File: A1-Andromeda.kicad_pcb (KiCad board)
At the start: 2 copper layers, 44 x 79.3 mm, 39 parts, among them J1 Conn_01x02, J2 Conn_01x02, J3 Conn_01x02, J5 Conn_01x10_Pin, J6 Conn_01x10_Pin, J8 Conn_01x10_Pin, SW1 SW_SPST, SW2 SW_DIP_x02, U1 LM2940IMPX-5.0/NOPB, U2 NUCLEO-F042K6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

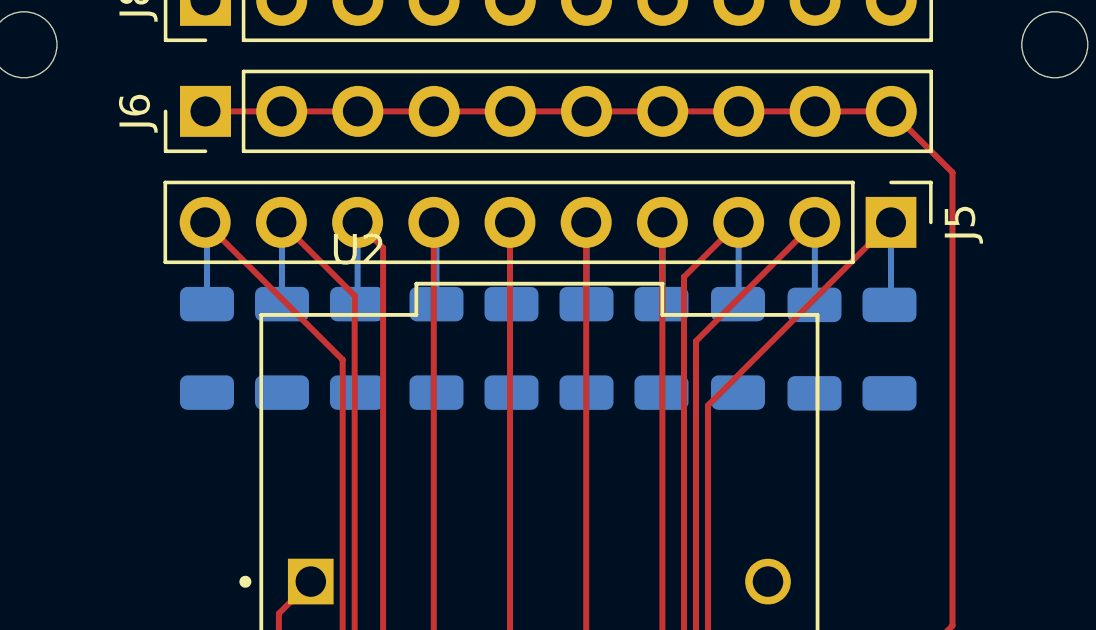
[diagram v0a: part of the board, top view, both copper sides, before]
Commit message: remove bypass capacitors
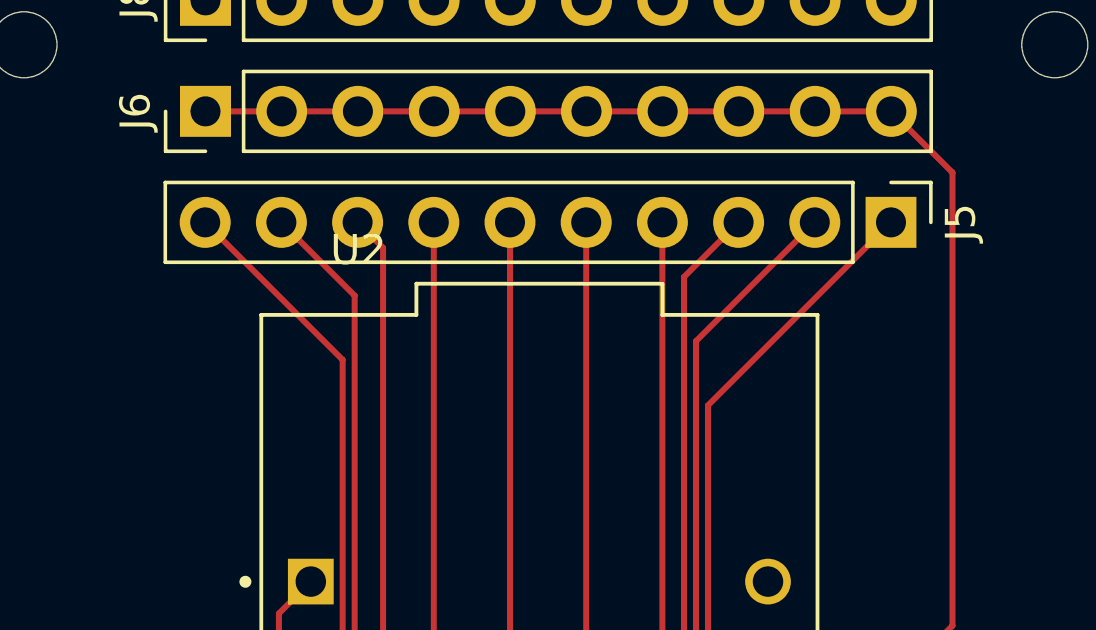
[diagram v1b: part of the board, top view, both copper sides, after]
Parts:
- removed C10, C11, C12, C13, C14, C15, C16, C17, C4, C6: 0.1uF, Capacitor_SMD:C_1206_3216Metric
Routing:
- net /A7: track 28.2 -> 25.5 mm
- net /A6: track 30.0 -> 27.3 mm
- net /A3: track 37.5 -> 34.8 mm
- net /D4: track 31.3 -> 28.6 mm
- net /D3: track 29.0 -> 26.3 mm
- net /A5: track 31.8 -> 29.1 mm
- net /A4: track 33.9 -> 31.2 mm
- net /D6: track 37.7 -> 35.0 mm
- net /D2: track 27.1 -> 24.5 mm
- net /D5: track 34.1 -> 31.5 mm

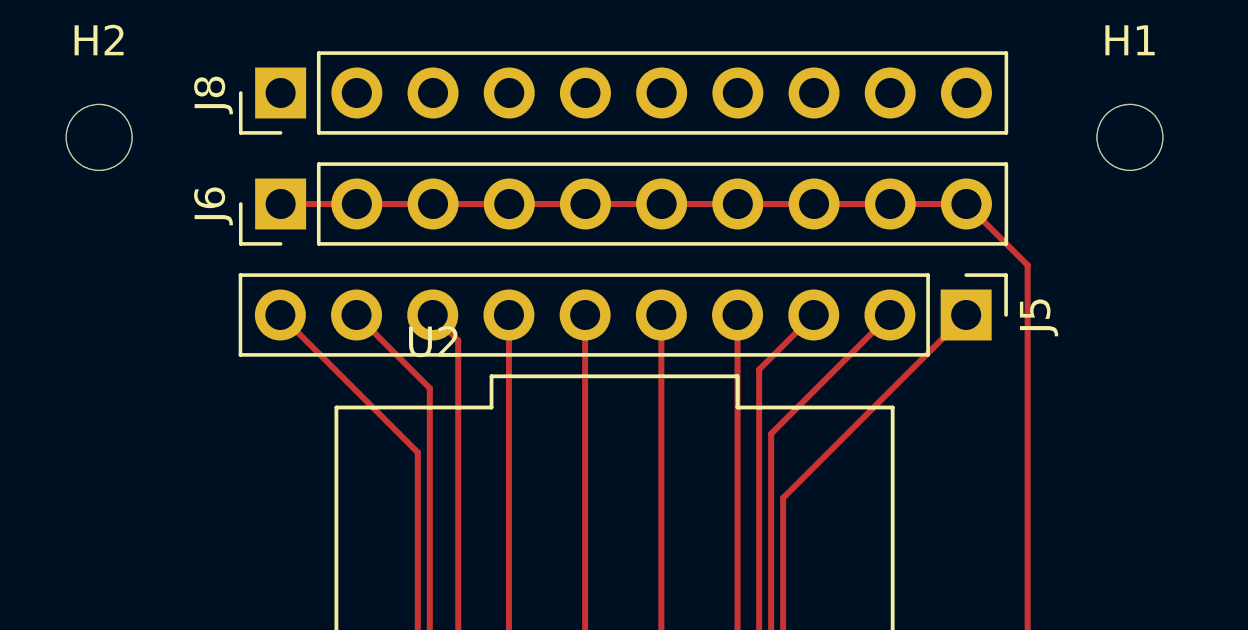
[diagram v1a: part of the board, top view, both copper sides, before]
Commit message: rotate GPIO pin array
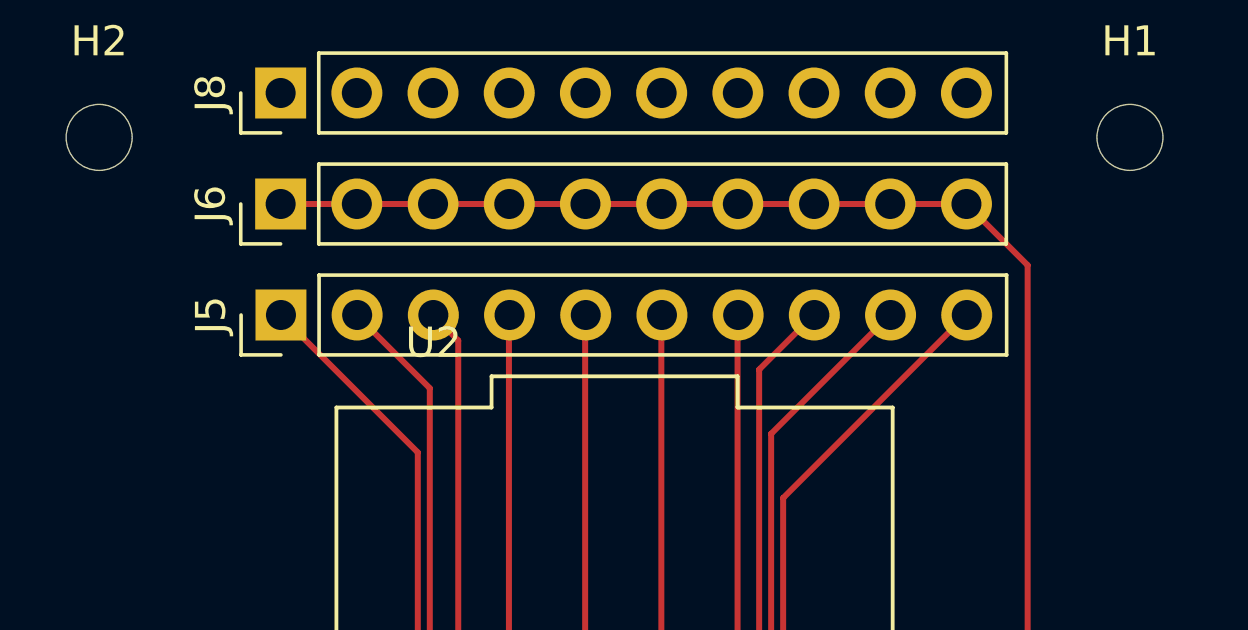
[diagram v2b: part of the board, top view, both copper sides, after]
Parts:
- moved J5 22.8 mm to (140.6, 64.9), turned to 90 degrees
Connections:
- J5 pad 1: /A7 -> /D2
- J5 pad 10: /D2 -> /A7
- J5 pad 2: /A6 -> /D3
- J5 pad 3: /A5 -> /D4
- J5 pad 4: /A4 -> /D5
- J5 pad 5: /A3 -> /D6
- J5 pad 6: /D6 -> /A3
- J5 pad 7: /D5 -> /A4
- J5 pad 8: /D4 -> /A5
- J5 pad 9: /D3 -> /A6
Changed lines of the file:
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@@
 	(footprint "Connector_PinHeader_2.54mm:PinHeader_1x10_P2.54mm_Vertical"
 		(layer "F.Cu")
-		(at 163.4 64.9 -90)
+		(at 140.56 64.9 90)
 		(descr "Through hole straight pin header, 1x10, 2.54mm pitch, single row")
 		(tags "Through hole pin header THT 1x10 2.54mm single row")
@@
 		)
 		(property "Footprint" "Connector_PinHeader_2.54mm:PinHeader_1x10_P2.54mm_Vertical"
-			(at 0 0 -90)
+			(at 0 0 90)
 			(unlocked yes)
 			(layer "F.Fab")
@@
 		)
 		(property "Datasheet" ""
-			(at 0 0 -90)
+			(at 0 0 90)
 			(unlocked yes)
 			(layer "F.Fab")
@@
 		)
 		(property "Description" "Generic connector, single row, 01x10, script generated"
-			(at 0 0 -90)
+			(at 0 0 90)
 			(unlocked yes)
 			(layer "F.Fab")
@@
 		(attr through_hole)
 		(fp_line
+			(start -1.33 -1.33)
+			(end 0 -1.33)
+			(stroke
+				(width 0.12)
+				(type solid)
+			)
+			(layer "F.SilkS")
+		)
+		(fp_line
+			(start -1.33 0)
+			(end -1.33 -1.33)
+			(stroke
+				(width 0.12)
+				(type solid)
+			)
+			(layer "F.SilkS")
+		)
+		(fp_line
+			(start 1.33 1.27)
+			(end 1.33 24.19)
+			(stroke
+				(width 0.12)
+				(type solid)
+			)
+			(layer "F.SilkS")
+		)
+		(fp_line
+			(start -1.33 1.27)
+			(end 1.33 1.27)
+			(stroke
+				(width 0.12)
+				(type solid)
+			)
+			(layer "F.SilkS")
+		)
+		(fp_line
+			(start -1.33 1.27)
+			(end -1.33 24.19)
+			(stroke
+				(width 0.12)
+				(type solid)
+			)
+			(layer "F.SilkS")
+		)
+		(fp_line
 			(start -1.33 24.19)
 			(end 1.33 24.19)
@@
 		)
 		(fp_line
-			(start -1.33 1.27)
-			(end -1.33 24.19)
-			(stroke
-				(width 0.12)
-				(type solid)
-			)
-			(layer "F.SilkS")
-		)
-		(fp_line
-			(start -1.33 1.27)
-			(end 1.33 1.27)
-			(stroke
-				(width 0.12)
-				(type solid)
-			)
-			(layer "F.SilkS")
-		)
-		(fp_line
-			(start 1.33 1.27)
-			(end 1.33 24.19)
-			(stroke
-				(width 0.12)
-				(type solid)
-			)
-			(layer "F.SilkS")
-		)
-		(fp_line
-			(start -1.33 0)
-			(end -1.33 -1.33)
-			(stroke
-				(width 0.12)
-				(type solid)
-			)
-			(layer "F.SilkS")
-		)
-		(fp_line
-			(start -1.33 -1.33)
-			(end 0 -1.33)
-			(stroke
-				(width 0.12)
-				(type solid)
-			)
-			(layer "F.SilkS")
+			(start 1.8 -1.8)
+			(end -1.8 -1.8)
+			(stroke
+				(width 0.05)
+				(type solid)
+			)
+			(layer "F.CrtYd")
+		)
+		(fp_line
+			(start -1.8 -1.8)
+			(end -1.8 24.65)
+			(stroke
+				(width 0.05)
+				(type solid)
+			)
+			(layer "F.CrtYd")
+		)
+		(fp_line
+			(start 1.8 24.65)
+			(end 1.8 -1.8)
+			(stroke
+				(width 0.05)
+				(type solid)
+			)
+			(layer "F.CrtYd")
 		)
 		(fp_line
@@
 		)
 		(fp_line
-			(start 1.8 24.65)
-			(end 1.8 -1.8)
-			(stroke
-				(width 0.05)
-				(type solid)
-			)
-			(layer "F.CrtYd")
-		)
-		(fp_line
-			(start -1.8 -1.8)
-			(end -1.8 24.65)
-			(stroke
-				(width 0.05)
-				(type solid)
-			)
-			(layer "F.CrtYd")
-		)
-		(fp_line
-			(start 1.8 -1.8)
-			(end -1.8 -1.8)
-			(stroke
-				(width 0.05)
-				(type solid)
-			)
-			(layer "F.CrtYd")
+			(start 1.27 -1.27)
+			(end 1.27 24.13)
+			(stroke
+				(width 0.1)
+				(type solid)
+			)
+			(layer "F.Fab")
+		)
+		(fp_line
+			(start -0.635 -1.27)
+			(end 1.27 -1.27)
+			(stroke
+				(width 0.1)
+				(type solid)
+			)
+			(layer "F.Fab")
+		)
+		(fp_line
+			(start -1.27 -0.635)
+			(end -0.635 -1.27)
+			(stroke
+				(width 0.1)
+				(type solid)
+			)
+			(layer "F.Fab")
+		)
+		(fp_line
+			(start 1.27 24.13)
+			(end -1.27 24.13)
+			(stroke
+				(width 0.1)
+				(type solid)
+			)
+			(layer "F.Fab")
 		)
 		(fp_line
@@
 			(layer "F.Fab")
 		)
-		(fp_line
-			(start 1.27 24.13)
-			(end -1.27 24.13)
-			(stroke
-				(width 0.1)
-				(type solid)
-			)
-			(layer "F.Fab")
-		)
-		(fp_line
-			(start -1.27 -0.635)
-			(end -0.635 -1.27)
-			(stroke
-				(width 0.1)
-				(type solid)
-			)
-			(layer "F.Fab")
-		)
-		(fp_line
-			(start -0.635 -1.27)
-			(end 1.27 -1.27)
-			(stroke
-				(width 0.1)
-				(type solid)
-			)
-			(layer "F.Fab")
-		)
-		(fp_line
-			(start 1.27 -1.27)
-			(end 1.27 24.13)
-			(stroke
-				(width 0.1)
-				(type solid)
-			)
-			(layer "F.Fab")
-		)
 		(fp_text user "${REFERENCE}"
-			(at 0 11.43 0)
+			(at 0 11.43 360)
 			(layer "F.Fab")
 			(effects
@@
 		)
 		(pad "1" thru_hole rect
-			(at 0 0 270)
+			(at 0 0 90)
+			(size 1.7 1.7)
+			(drill 1)
+			(layers "*.Cu" "*.Mask")
+			(remove_unused_layers no)
+			(net 11 "/D2")
+			(pinfunction "Pin_1")
+			(pintype "passive")
+		)
+		(pad "2" thru_hole oval
+			(at 0 2.54 90)
+			(size 1.7 1.7)
+			(drill 1)
+			(layers "*.Cu" "*.Mask")
+			(remove_unused_layers no)
+			(net 12 "/D3")
+			(pinfunction "Pin_2")
+			(pintype "passive")
+		)
+		(pad "3" thru_hole oval
+			(at 0 5.08 90)
+			(size 1.7 1.7)
+			(drill 1)
+			(layers "*.Cu" "*.Mask")
+			(remove_unused_layers no)
+			(net 17 "/D4")
+			(pinfunction "Pin_3")
+			(pintype "passive")
+		)
+		(pad "4" thru_hole oval
+			(at 0 7.62 90)
+			(size 1.7 1.7)
+			(drill 1)
+			(layers "*.Cu" "*.Mask")
+			(remove_unused_layers no)
+			(net 18 "/D5")
+			(pinfunction "Pin_4")
+			(pintype "passive")
+		)
+		(pad "5" thru_hole oval
+			(at 0 10.16 90)
+			(size 1.7 1.7)
+			(drill 1)
+			(layers "*.Cu" "*.Mask")
+			(remove_unused_layers no)
+			(net 39 "/D6")
+			(pinfunction "Pin_5")
+			(pintype "passive")
+		)
+		(pad "6" thru_hole oval
+			(at 0 12.7 90)
+			(size 1.7 1.7)
+			(drill 1)
+			(layers "*.Cu" "*.Mask")
+			(remove_unused_layers no)
+			(net 10 "/A3")
+			(pinfunction "Pin_6")
+			(pintype "passive")
+		)
+		(pad "7" thru_hole oval
+			(at 0 15.24 90)
+			(size 1.7 1.7)
+			(drill 1)
+			(layers "*.Cu" "*.Mask")
+			(remove_unused_layers no)
+			(net 13 "/A4")
+			(pinfunction "Pin_7")
+			(pintype "passive")
+		)
+		(pad "8" thru_hole oval
+			(at 0 17.78 90)
+			(size 1.7 1.7)
+			(drill 1)
+			(layers "*.Cu" "*.Mask")
+			(remove_unused_layers no)
+			(net 9 "/A5")
+			(pinfunction "Pin_8")
+			(pintype "passive")
+		)
+		(pad "9" thru_hole oval
+			(at 0 20.32 90)
+			(size 1.7 1.7)
+			(drill 1)
+			(layers "*.Cu" "*.Mask")
+			(remove_unused_layers no)
+			(net 19 "/A6")
+			(pinfunction "Pin_9")
+			(pintype "passive")
+		)
+		(pad "10" thru_hole oval
+			(at 0 22.86 90)
 			(size 1.7 1.7)
 			(drill 1)
@@
 			(remove_unused_layers no)
 			(net 16 "/A7")
-			(pinfunction "Pin_1")
-			(pintype "passive")
-		)
-		(pad "2" thru_hole oval
-			(at 0 2.54 270)
-			(size 1.7 1.7)
-			(drill 1)
-			(layers "*.Cu" "*.Mask")
-			(remove_unused_layers no)
-			(net 19 "/A6")
-			(pinfunction "Pin_2")
-			(pintype "passive")
-		)
-		(pad "3" thru_hole oval
-			(at 0 5.08 270)
-			(size 1.7 1.7)
-			(drill 1)
-			(layers "*.Cu" "*.Mask")
-			(remove_unused_layers no)
-			(net 9 "/A5")
-			(pinfunction "Pin_3")
-			(pintype "passive")
-		)
-		(pad "4" thru_hole oval
-			(at 0 7.62 270)
-			(size 1.7 1.7)
-			(drill 1)
-			(layers "*.Cu" "*.Mask")
-			(remove_unused_layers no)
-			(net 13 "/A4")
-			(pinfunction "Pin_4")
-			(pintype "passive")
-		)
-		(pad "5" thru_hole oval
-			(at 0 10.16 270)
-			(size 1.7 1.7)
-			(drill 1)
-			(layers "*.Cu" "*.Mask")
-			(remove_unused_layers no)
-			(net 10 "/A3")
-			(pinfunction "Pin_5")
-			(pintype "passive")
-		)
-		(pad "6" thru_hole oval
-			(at 0 12.7 270)
-			(size 1.7 1.7)
-			(drill 1)
-			(layers "*.Cu" "*.Mask")
-			(remove_unused_layers no)
-			(net 39 "/D6")
-			(pinfunction "Pin_6")
-			(pintype "passive")
-		)
-		(pad "7" thru_hole oval
-			(at 0 15.24 270)
-			(size 1.7 1.7)
-			(drill 1)
-			(layers "*.Cu" "*.Mask")
-			(remove_unused_layers no)
-			(net 18 "/D5")
-			(pinfunction "Pin_7")
-			(pintype "passive")
-		)
-		(pad "8" thru_hole oval
-			(at 0 17.78 270)
-			(size 1.7 1.7)
-			(drill 1)
-			(layers "*.Cu" "*.Mask")
-			(remove_unused_layers no)
-			(net 17 "/D4")
-			(pinfunction "Pin_8")
-			(pintype "passive")
-		)
-		(pad "9" thru_hole oval
-			(at 0 20.32 270)
-			(size 1.7 1.7)
-			(drill 1)
-			(layers "*.Cu" "*.Mask")
-			(remove_unused_layers no)
-			(net 12 "/D3")
-			(pinfunction "Pin_9")
-			(pintype "passive")
-		)
-		(pad "10" thru_hole oval
-			(at 0 22.86 270)
-			(size 1.7 1.7)
-			(drill 1)
-			(layers "*.Cu" "*.Mask")
-			(remove_unused_layers no)
-			(net 11 "/D2")
 			(pinfunction "Pin_10")
 			(pintype "passive")

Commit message: fix ground plane
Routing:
- net GND: track 13.4 -> 1.12 mm
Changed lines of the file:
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@@
 		)
 		(fp_text user "${REFERENCE}"
-			(at 0 11.43 360)
+			(at 0 11.43 0)
 			(layer "F.Fab")
 			(effects
@@
 	)
 	(segment
-		(start 134.26 96.555)
-		(end 137.615 93.2)
-		(width 2)
-		(layer "B.Cu")
-		(net 38)
-	)
-	(segment
-		(start 167.965 93.2)
-		(end 169.55 93.2)
-		(width 2)
-		(layer "B.Cu")
-		(net 38)
-	)
-	(segment
-		(start 137.615 93.2)
-		(end 139 93.2)
-		(width 2)
-		(layer "B.Cu")
-		(net 38)
-	)
-	(segment
-		(start 164.76 96.405)
-		(end 167.965 93.2)
-		(width 2)
-		(layer "B.Cu")
-		(net 38)
-	)
-	(segment
 		(start 150.7 64.9)
 		(end 150.7 90.554)
@@
 		(polygon
 			(pts
-				(xy 165.1 97.525) (xy 165.1 95.2) (xy 164.45 95.225) (xy 164.425 97.525)
+				(xy 165.1 97.525) (xy 165.1 95.2) (xy 164.45 95.2) (xy 164.425 97.525)
 			)
 		)
@@
 			)
 		)
-	)
-	(zone
-		(net 0)
-		(net_name "")
-		(layer "B.Cu")
-		(hatch edge 0.5)
-		(connect_pads yes
-			(clearance 0)
-		)
-		(min_thickness 0.25)
-		(filled_areas_thickness no)
-		(keepout
-			(tracks allowed)
-			(vias allowed)
-			(pads allowed)
-			(copperpour not_allowed)
-			(footprints allowed)
-		)
-		(fill
-			(thermal_gap 0.5)
-			(thermal_bridge_width 0.5)
-			(island_removal_mode 1)
-			(island_area_min 10)
-		)
-		(polygon
-			(pts
-				(xy 170.65 94.325) (xy 168.55 94.325) (xy 165.25 97.625) (xy 163.85 97.275) (xy 163.55 95.975) (xy 167.4 92.125)
-				(xy 167.75 92.125) (xy 170.65 92.125)
-			)
-		)
-	)
-	(zone
-		(net 0)
-		(net_name "")
-		(layer "B.Cu")
-		(hatch edge 0.5)
-		(connect_pads yes
-			(clearance 0)
-		)
-		(min_thickness 0.25)
-		(filled_areas_thickness no)
-		(keepout
-			(tracks allowed)
-			(vias allowed)
-			(pads allowed)
-			(copperpour not_allowed)
-			(footprints allowed)
-		)
-		(fill
-			(thermal_gap 0.5)
-			(thermal_bridge_width 0.5)
-			(island_removal_mode 1)
-			(island_area_min 10)
-		)
-		(polygon
-			(pts
-				(xy 140.15 94.475) (xy 138.05 94.475) (xy 134.55 97.9) (xy 133.45 97.475) (xy 132.85 96.35) (xy 136.8 92.375)
-				(xy 137.3 92.025) (xy 140.2 92.025)
-			)
-		)

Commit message: redo PCB
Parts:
- moved H4 85.7 mm to (104.2, 71.9)
- moved H3 79.2 mm to (190.2, 71.9)
- moved H1 77.6 mm to (104.2, 101.9)
- moved H2 70.3 mm to (190.2, 101.9)
- moved J1 67.9 mm to (111.1, 81.2), turned to 0 degrees
- moved C3 61.6 mm to (117.0, 75.6), turned to 180 degrees
- moved C1 60.9 mm to (185.1, 85.1)
- moved SW1 58.6 mm to (123.9, 74.3), turned to 90 degrees
- moved U1 55.6 mm to (187.2, 90.0), turned to 0 degrees
- moved C2 52.0 mm to (185.1, 94.9), turned to 0 degrees
- moved F1 50.3 mm to (117.0, 73.1)
- moved TP2 40.2 mm to (168.2, 75.3)
- moved SW2 34.6 mm to (177.3, 98.2), turned to 180 degrees
- moved TP1 32.6 mm to (184.3, 82.2)
- moved R2 30.4 mm to (179.9, 75.6), turned to 0 degrees
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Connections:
- J5 pad 1: /D2 -> /D6
- J5 pad 2: /D3 -> /D5
- J5 pad 4: /D5 -> /D3
- J5 pad 5: /D6 -> /D2
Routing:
- net +5V: track 136.4 -> 79.4 mm, vias 1 -> 2
- net +12V: track 82.9 -> 121.2 mm
- net /D6: track 35.0 -> 4.46 mm
- net /L_MOTOR_IN2: track 11.4 -> 38.7 mm, vias 2 -> 0
- net /D5: track 31.5 -> 4.46 mm
- net /R_MOTOR_IN2: track 47.8 -> 22.3 mm
- net /D4: track 28.6 -> 4.46 mm
- net /R_MOTOR_IN1: track 47.2 -> 23.6 mm
- net /L_MOTOR_IN1: track 11.5 -> 34.0 mm
- net /D3: track 26.3 -> 4.46 mm
- net /D2: track 24.5 -> 4.46 mm
- net /DIP_SWITCH_OUT1: track 38.2 -> 55.8 mm, vias 4 -> 0
- net /DIP_SWITCH_OUT2: track 39.1 -> 50.6 mm, vias 4 -> 0
- net Net-(J3-Pin_1): track 15.3 -> 4.66 mm
- net /A3: track 34.8 -> 25.0 mm
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- removed copper zone on F.Cu, net Net-(U3-ILIM)
- removed copper zone on F.Cu, net Net-(U4-ILIM)
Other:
- board size 44 x 79.3 mm -> 96 x 40 mm

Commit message: update silkscreen
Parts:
- moved GND 50.0 mm to (184.0, 69.2)
- moved SW2 35.7 mm to (141.8, 102.8)
- moved 12V 14.0 mm to (179.0, 69.2)
- moved 5V 8.38 mm to (174.0, 69.2)
- moved J1 1.91 mm to (109.2, 81.0)
- moved J3 0.79 mm to (176.8, 87.5)
- moved C8 0.79 mm to (172.5, 82.3)
- moved J5 0.79 mm to (140.8, 77.4)
- moved J6 0.79 mm to (140.8, 73.7)
- moved J8 0.79 mm to (140.8, 69.9)
- moved U4 0.79 mm to (179.2, 80.7)
- moved C5 0.79 mm to (116.6, 100.4)
- moved R1 0.79 mm to (110.9, 103.4)
- moved C3 0.79 mm to (116.3, 75.2)
- moved F1 0.79 mm to (116.3, 72.7)
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- renumbered TP1 to 12V, TP2 to 5V, TP3 to GND
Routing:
- net /DIP_SWITCH_OUT1: track 55.8 -> 23.4 mm
- net /DIP_SWITCH_OUT2: track 50.6 -> 20.0 mm
- net +5V: track 79.4 -> 99.8 mm, vias 2 -> 4
- net +12V: track 121.2 -> 126.9 mm
- net (no net): track 5.37 -> 0.00 mm
- net /R_MOTOR_IN2: track 22.3 -> 21.5 mm
- net Net-(J2-Pin_2): track 10.4 -> 9.67 mm
- net /R_MOTOR_IN1: track 23.6 -> 22.9 mm
- net Net-(J1-Pin_2): track 12.5 -> 13.2 mm
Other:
- board text added: "5V"
- board text added: "A3"
- board text added: "A4"
- board text added: "A5"
- board text added: "A6"
- board text added: "A7"
- board text added: "D2"
- board text added: "D3"
- board text added: "D4"
- board text added: "D5"
- board text added: "D6"
- board text added: "GND"
- board text added: "GPIO"
- board text added: "L"
- board text added: "MODE"
- board text added: "R"

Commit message: finish up
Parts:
- added D1: GREEN, LED_SMD:LED_1206_3216Metric, F.Cu at (113.9, 69.6)
- added J4: Conn_01x03_Socket, Connector_PinSocket_2.54mm:PinSocket_1x03_P2.54mm_Vertical, F.Cu at (129.3, 102.0)
- added R3: 100K, Capacitor_SMD:C_1206_3216Metric, F.Cu at (134.6, 101.5)
- added R4: 100K, Capacitor_SMD:C_1206_3216Metric, F.Cu at (134.6, 103.9)
- added R5: 220, Resistor_SMD:R_1206_3216Metric, F.Cu at (116.3, 69.6)
- moved R2 28.8 mm to (174.7, 103.7), turned to 180 degrees
- moved C7 23.6 mm to (180.5, 100.8), turned to 180 degrees
- moved U4 18.1 mm to (174.8, 98.3), turned to 90 degrees
- moved C8 17.0 mm to (181.5, 96.7), turned to 180 degrees
- moved J1 5.64 mm to (104.3, 78.2)
- moved F1 3.92 mm to (118.7, 69.6), turned to 90 degrees
- moved TP1 1.80 mm to (180.2, 70.6)
- moved TP2 1.80 mm to (175.2, 70.6)
- moved TP3 1.80 mm to (185.2, 70.6)
- moved C3 1.19 mm to (117.5, 75.2)
- moved H2 1.19 mm to (191.4, 101.9)
- moved H3 1.19 mm to (191.4, 71.9)
- moved J3 1.19 mm to (178.0, 87.5)
- moved J5 1.19 mm to (142.0, 77.4)
- moved J6 1.19 mm to (142.0, 73.7)
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- renumbered 12V to TP1, 5V to TP2, GND to TP3
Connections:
- U2 pad CN3_14: unconnected-(U2-PB5/D11-PadCN3_14) -> /SRT_STP_MODULE
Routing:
- net +5V: track 99.8 -> 148.3 mm, vias 4 -> 0
- net /SRT_STP_MODULE: track 0.00 -> 31.7 mm
- net /R_MOTOR_IN1: track 22.9 -> 37.9 mm
- net /R_MOTOR_IN2: track 21.5 -> 35.4 mm
- net Net-(J3-Pin_2): track 9.67 -> 22.9 mm
- net Net-(J3-Pin_1): track 4.65 -> 8.94 mm
- net Net-(J1-Pin_2): track 13.2 -> 16.9 mm
- net GND: track 1.17 -> 4.78 mm, vias 52 -> 51
- net Net-(U4-ILIM): track 2.84 -> 0.00 mm
- net /L_MOTOR_IN1: track 34.0 -> 36.7 mm, vias 2 -> 0
- net Net-(SW1-B): track 11.4 -> 13.9 mm
- net Net-(D1-A): track 0.00 -> 2.34 mm
- net /DIP_SWITCH_OUT2: track 20.0 -> 22.2 mm
- net /DIP_SWITCH_OUT1: track 23.4 -> 25.4 mm
- net +12V: track 126.9 -> 128.7 mm
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- added copper zone on F.Cu, net Net-(U3-ILIM)
- added copper zone on F.Cu, net Net-(U4-ILIM)
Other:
- outline, holes or cut-outs redrawn
- board text added: "A1 {dblquote}Andromeda{dblquote} Nathan Wignall 03/26/25"
- board text added: "BATTERY"
- board text added: "L_MOTOR"
- board text added: "R_MOTOR"
- board text added: "SRT/STP"
